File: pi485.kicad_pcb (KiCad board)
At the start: 2 copper layers, 48 x 70 mm, 29 parts, among them J1 RS485, P1 Rasperry Pi, P2 PWR, P3 Term, Q1 2N2222, Q2 2N2222, Q3 2N2222, U1 NE555, U2 MAX485

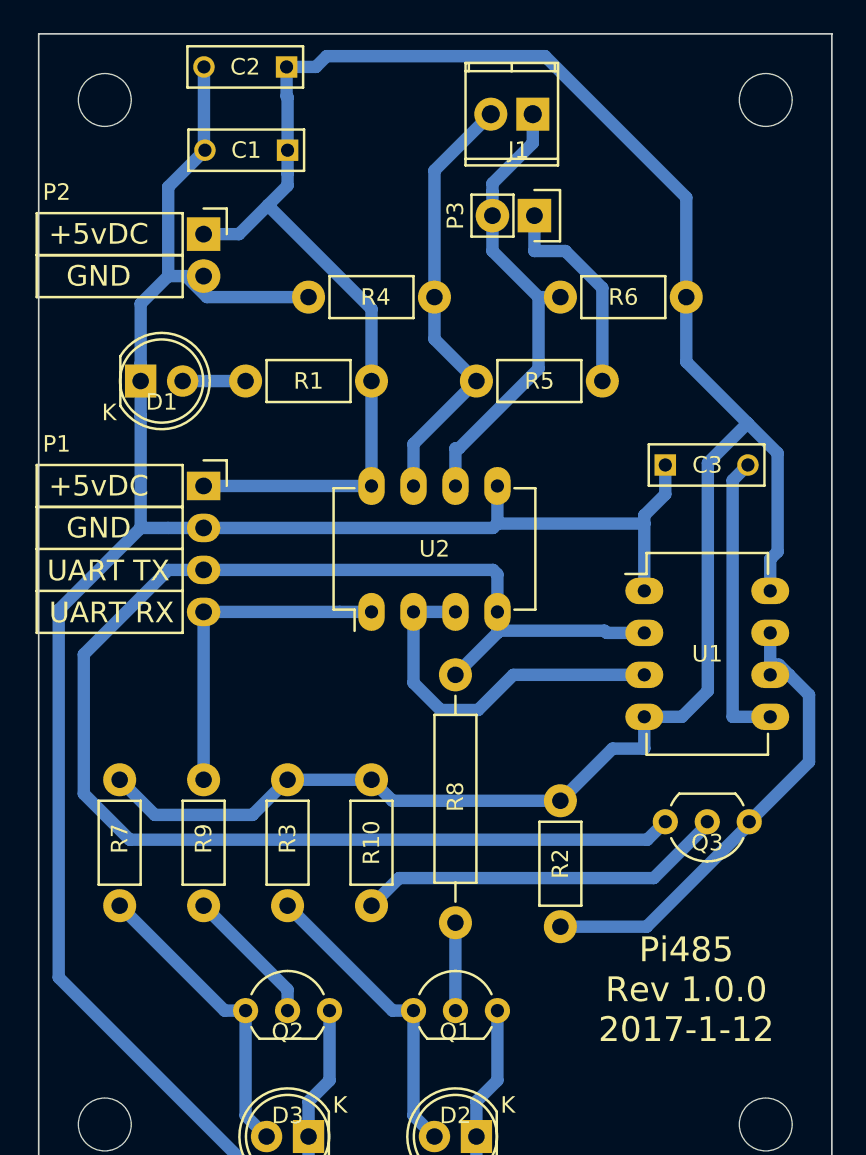
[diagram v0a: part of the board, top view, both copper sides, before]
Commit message: Resistor / LED adjustments, BAT43 restoration (digi-key order placed). Footprint updates.
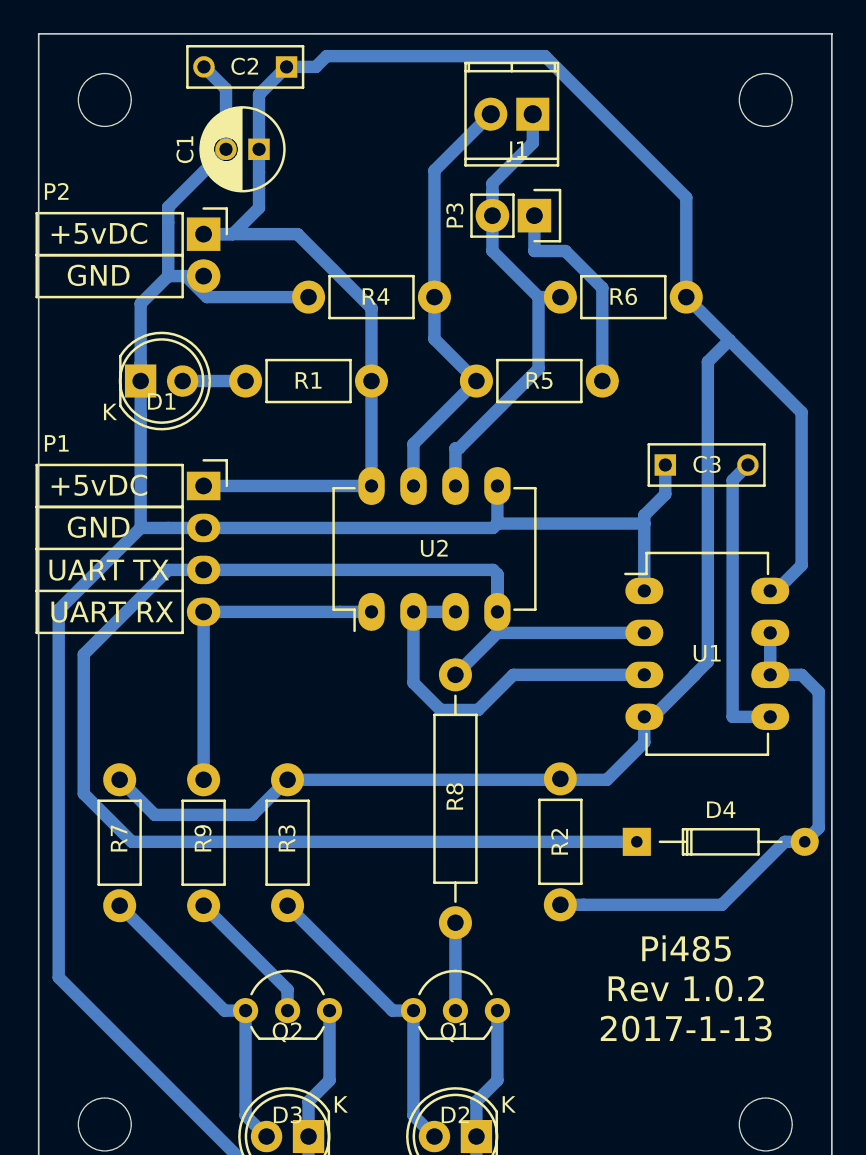
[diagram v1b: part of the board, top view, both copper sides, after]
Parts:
- removed Q3: 2N2222, TO_SOT_Packages_THT:TO-92_Inline_Wide
- removed R10: 2.5k, Resistors_THT:Resistor_Horizontal_RM7mm
- added D4: BAT43, Diodes_THT:Diode_DO-35_SOD27_Horizontal_RM10, F.Cu at (120.2, 107.9)
- C1: footprint Capacitors_THT:C_Rect_L7_W2.5_P5 -> Capacitors_THT:C_Radial_D5_L11_P2
- D1: value PWRLED -> PWR
- D2: value TXLED -> TX
- D3: value RXLED -> RX
- Q1, Q2: value 2N2222 -> 2N4401
- R1: value 1k -> 120
- R3, R7: value 220 -> 200
- R8, R9: value 2.5k -> 270
- moved C1 1.73 mm to (97.3, 66.0)
- moved R2 1.33 mm to (115.6, 111.7)
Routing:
- net Net-(Q3-Pad2): track 22.5 -> 0.00 mm
- net VCC: track 156.5 -> 163.2 mm
- net Net-(D4-Pad2): track 29.5 -> 31.1 mm
- net GND: track 160.8 -> 161.8 mm
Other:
- board text added: "Pi485 Rev 1.0.2 2017-1-13"
- board text removed: "Pi485 Rev 1.0.0 2017-1-12"

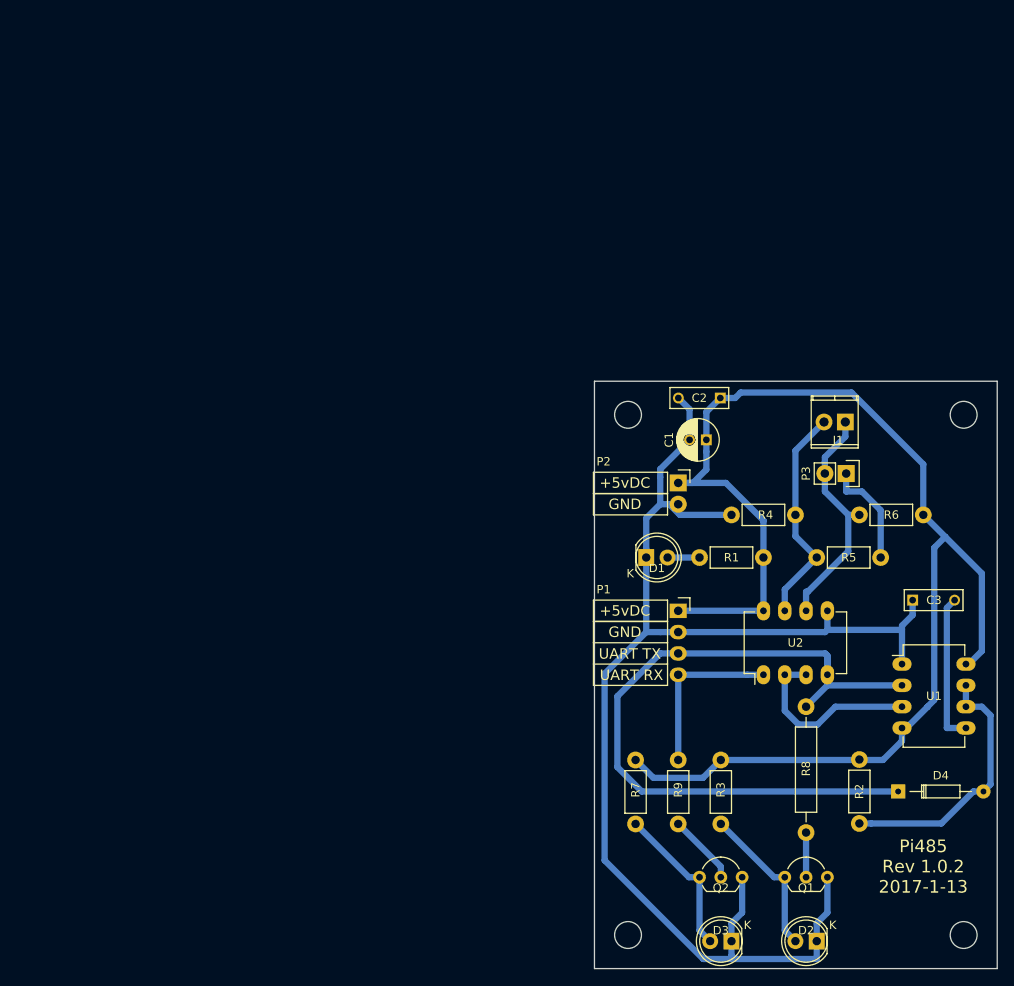
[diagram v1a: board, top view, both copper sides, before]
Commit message: Updated the PCB, tweaked some routes and pad sizes.
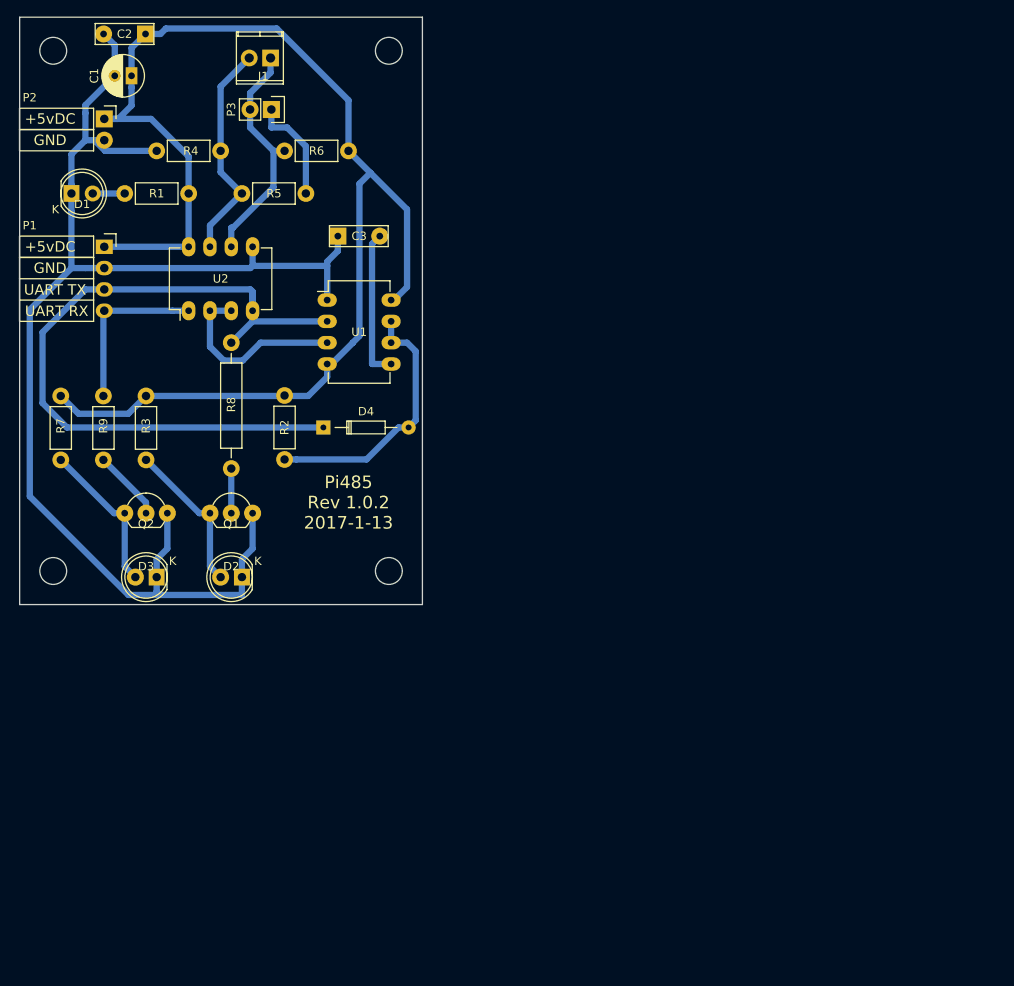
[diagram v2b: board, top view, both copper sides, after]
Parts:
- moved J1 81.1 mm to (45.4, 20.5)
- moved Q1 81.1 mm to (38.2, 74.7)
- moved R7 81.1 mm to (20.4, 68.4)
- moved R9 81.1 mm to (25.5, 68.4)
- moved C1 81.1 mm to (28.8, 22.6)
- moved C2 81.1 mm to (30.5, 17.6)
- moved C3 81.1 mm to (53.4, 41.7)
- moved D1 81.1 mm to (21.7, 36.6)
- moved D2 81.1 mm to (42.0, 82.3)
- moved D3 81.1 mm to (31.8, 82.3)
- moved D4 81.1 mm to (51.7, 64.5)
- moved P3 81.1 mm to (45.5, 26.6)
- moved Q2 81.1 mm to (28.0, 74.7)
- moved R1 81.1 mm to (35.6, 36.6)
- moved R3 81.1 mm to (30.6, 68.4)
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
